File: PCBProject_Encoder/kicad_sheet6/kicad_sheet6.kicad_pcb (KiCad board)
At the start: 4 copper layers, 77.4 x 89.8 mm, 145 parts, among them J1 L77HDE15SD1CH4RHNVGA, J2 HIF3FC-10PA-2.54DSA, U1 DS3486M, U2 DS3486M, U3 SN74HC365D

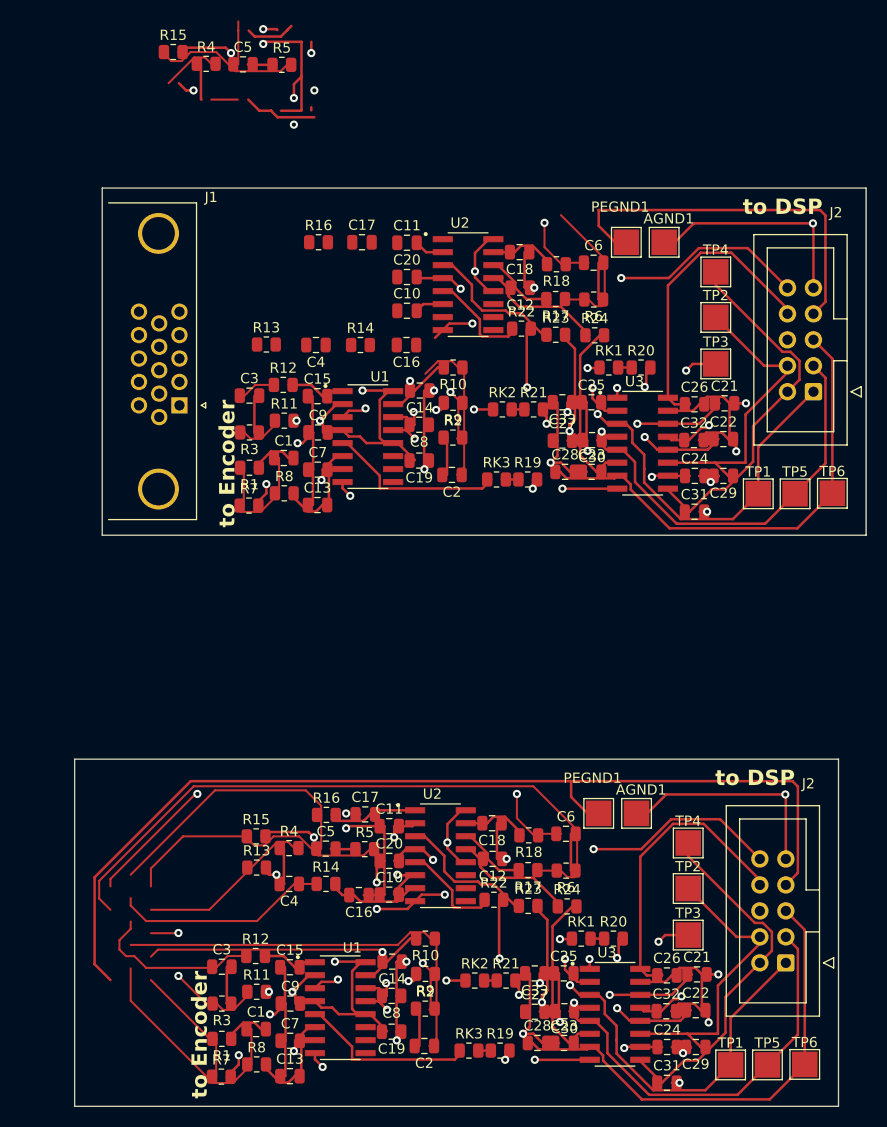
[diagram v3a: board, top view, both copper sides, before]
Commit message: 01.29pcb更改
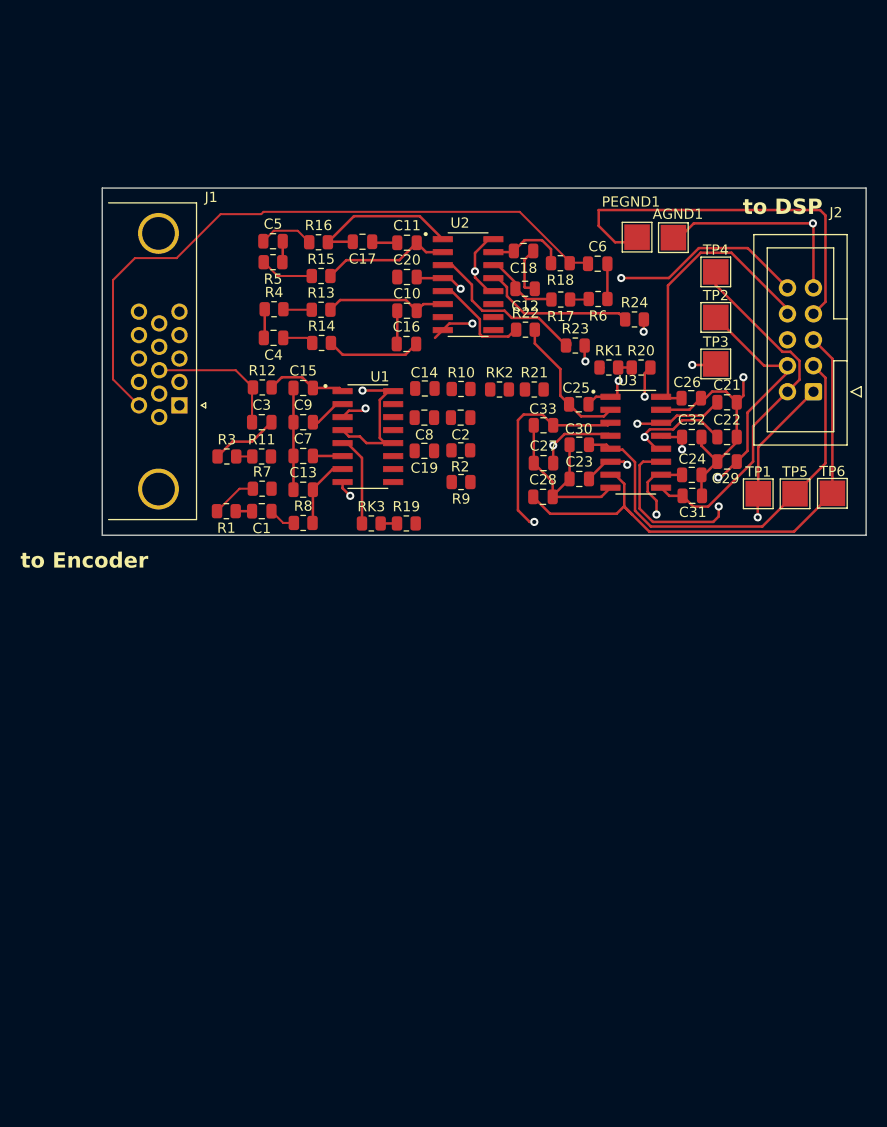
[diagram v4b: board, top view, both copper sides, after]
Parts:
- removed the AGND1 at (110.9, 153.1)
- removed the C1 at (73.7, 174.2)
- removed the C10 at (86.7, 161.0)
- removed the C11 at (86.7, 154.3)
- removed the C12 at (96.8, 157.5)
- removed the C13 at (77.0, 178.8)
- removed the C14 at (87.0, 167.6)
- removed the C15 at (77.0, 168.1)
- removed the C16 at (83.8, 161.0)
- removed the C17 at (84.4, 153.2)
- removed the C18 at (96.8, 154.0)
- removed the C19 at (87.0, 174.4)
- removed the C2 at (90.2, 175.8)
- removed the C20 at (86.7, 157.7)
- removed the C21 at (116.8, 168.8)
- removed the C22 at (116.7, 172.3)
- removed the C23 at (103.8, 175.5)
- removed the C24 at (113.9, 175.9)
- removed the C25 at (103.8, 168.7)
- removed the C26 at (113.9, 168.9)
- removed the C27 at (101.0, 172.4)
- removed the C28 at (101.2, 175.5)
- removed the C29 at (116.7, 175.9)
- removed the C3 at (70.3, 168.1)
- removed the C30 at (103.8, 172.4)
- removed the C31 at (113.9, 179.4)
- removed the C32 at (113.8, 172.4)
- removed the C33 at (101.0, 168.7)
- removed the C4 at (76.9, 160.0)
- removed the C5 at (80.5, 156.5)
- removed the C6 at (104.0, 155.1)
- removed the C7 at (77.0, 175.3)
- removed the C8 at (87.0, 170.9)
- removed the C9 at (77.0, 171.7)
- removed the J2 at (125.5, 167.7)
- removed the PEGND1 at (107.2, 153.1)
- removed the R1 at (70.3, 175.1)
- removed the R10 at (90.3, 165.3)
- removed the R11 at (73.8, 170.5)
- removed the R12 at (73.7, 167.0)
- removed the R13 at (73.8, 158.3)
- removed the R14 at (80.5, 160.0)
- removed the R15 at (73.7, 155.3)
- removed the R16 at (80.6, 153.2)
- removed the R17 at (100.3, 158.6)
- removed the R18 at (100.4, 155.2)
- removed the R19 at (97.6, 176.2)
- removed the R2 at (90.2, 172.2)
- removed the R20 at (108.6, 165.3)
- removed the R21 at (98.1, 169.4)
- removed the R22 at (97.0, 161.5)
- removed the R23 at (100.3, 162.1)
- removed the R24 at (104.1, 162.2)
- removed the R3 at (70.3, 171.7)
- removed the R4 at (76.9, 156.5)
- removed the R5 at (84.3, 156.6)
- removed the R6 at (104.0, 158.7)
- removed the R7 at (70.3, 178.8)
- removed the R8 at (73.8, 177.6)
- removed the R9 at (90.3, 168.8)
- removed the RK1 at (105.5, 165.3)
- removed the RK2 at (95.1, 169.4)
- removed the RK3 at (94.5, 176.2)
- removed the TP1 at (120.1, 177.7)
- removed the TP2 at (116.0, 160.4)
- removed the TP3 at (116.0, 164.9)
- removed the TP4 at (116.0, 155.9)
- removed the TP5 at (123.7, 177.7)
- removed the TP6 at (127.3, 177.6)
- removed the U1 at (81.9, 172.1)
- removed the U2 at (91.7, 157.2)
- removed the U3 at (108.8, 172.7)
- moved R15 26.2 mm to (80.0, 100.5)
- moved R4 24.9 mm to (75.5, 103.8)
- moved R5 19.3 mm to (75.3, 99.2), turned to 180 degrees
- moved C5 17.5 mm to (75.3, 97.1)
- moved RK3 13.0 mm to (85.0, 124.7)
- moved R19 12.6 mm to (88.4, 124.7)
- moved R9 7.79 mm to (93.7, 120.7)
- moved R13 6.34 mm to (80.0, 103.8)
- moved C2 5.66 mm to (93.7, 114.3)
- moved C1 5.63 mm to (74.2, 123.5), turned to 180 degrees
- moved R1 4.81 mm to (70.8, 123.5)
- moved C4 4.21 mm to (75.4, 106.5)
- moved R24 4.19 mm to (110.7, 104.8)
- moved R11 4.14 mm to (74.2, 118.2)
- moved R14 3.81 mm to (80.1, 107.0)
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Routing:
- net AGND: track 500.7 -> 160.3 mm, vias 38 -> 5
- net D+5V: track 206.0 -> 82.3 mm, vias 8 -> 4
- net PE_GND: track 136.0 -> 37.4 mm
- net /HALL_W+: track 79.7 -> 1.85 mm
- net /ENCB-: track 56.2 -> 0.00 mm
- net Net-(U1-OUT_B): track 52.7 -> 0.07 mm, vias 4 -> 0
- net /ENCB+: track 42.0 -> 0.00 mm, vias 4 -> 0
- net /QEP1_HALL_W: track 94.6 -> 53.7 mm
- net /QEP1_HALL_V: track 78.7 -> 41.1 mm
- net /MQEP1A: track 71.3 -> 35.9 mm
- net /HALL_V+: track 40.3 -> 5.26 mm
- net VDD: track 58.6 -> 28.8 mm
- net Net-(U3-6A): track 38.9 -> 9.32 mm, vias 4 -> 1
- net Net-(U1-OUT_A): track 32.0 -> 3.42 mm, vias 4 -> 1
- net /ENCA-: track 30.5 -> 2.66 mm
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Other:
- board size 77.4 x 89.8 mm -> 74.7 x 33.9 mm

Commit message: renew Encoder--kicad_sheet6
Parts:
- moved R19 73.6 mm to (149.8, 84.1), turned to -90 degrees
- moved RK3 61.1 mm to (131.8, 85.4), turned to -90 degrees
- moved PEGND1 59.5 mm to (167.1, 77.1)
- moved R3 59.3 mm to (116.7, 80.6), turned to -90 degrees
- moved R11 58.2 mm to (118.7, 80.6), turned to 90 degrees
- moved R1 58.1 mm to (112.9, 83.4)
- moved C19 57.3 mm to (129.0, 75.5)
- moved C3 57.0 mm to (116.6, 76.6), turned to -90 degrees
- moved R7 56.7 mm to (116.4, 83.3)
- moved R12 56.4 mm to (118.7, 76.6), turned to -90 degrees
- moved R9 56.3 mm to (134.0, 81.3), turned to 90 degrees
- moved C2 56.1 mm to (135.8, 77.2), turned to -90 degrees
- moved R2 55.7 mm to (136.0, 81.3), turned to -90 degrees
- moved C15 55.0 mm to (120.9, 76.6), turned to -90 degrees
- moved C13 55.0 mm to (120.4, 86.1)
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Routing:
- net AGND: track 160.3 -> 90.7 mm, vias 5 -> 18
- net D+5V: track 82.3 -> 142.0 mm, vias 4 -> 0
- net /ENCB-: track 0.00 -> 50.5 mm, vias 0 -> 1
- net /HALL_W+: track 1.85 -> 45.7 mm, vias 0 -> 1
- net /ENCB+: track 0.00 -> 41.1 mm, vias 0 -> 1
- net /HALL_W-: track 64.5 -> 33.4 mm
- net /HALL_U-: track 3.04 -> 31.5 mm, vias 0 -> 1
- net PE_GND: track 37.4 -> 10.9 mm
- net Net-(U3-4A): track 31.7 -> 6.71 mm, vias 1 -> 0
- net /QEP1_HALL_U: track 58.2 -> 35.0 mm
- net /ENCZ+: track 1.58 -> 20.3 mm
- net Net-(R19-Pad1): track 1.60 -> 20.3 mm
- net /ENCZ-: track 13.3 -> 31.0 mm
- net /QEP1_HALL_W: track 53.7 -> 37.1 mm, vias 0 -> 1
- net /MQEP1A: track 35.9 -> 19.5 mm
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- added copper zone on In1.Cu, net AGND
- added copper zone on In2.Cu, net PE_GND
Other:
- board size 74.7 x 33.9 mm -> 73.4 x 33.3 mm
